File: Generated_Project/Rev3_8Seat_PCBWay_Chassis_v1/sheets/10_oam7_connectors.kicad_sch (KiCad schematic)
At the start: 0 parts

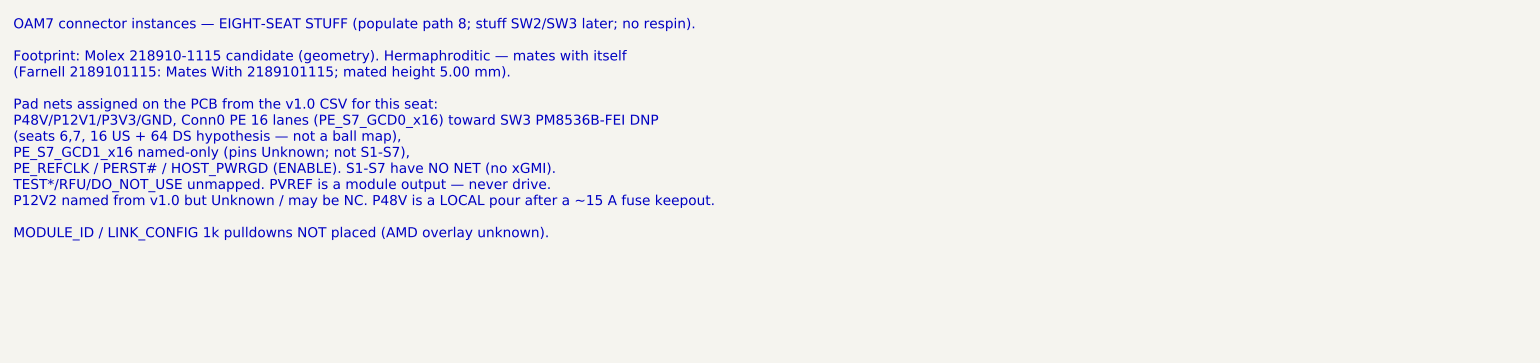
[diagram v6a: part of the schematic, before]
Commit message: Retarget Rev3 first article to seats 0-1 GCD0 x16 (2-module path).
Same 8-seat PCB. Without overlay, 2x MI250X means two modules can sit
and at most GCD0 on each can be named toward the host keepout (2 GCDs),
not 2x full-width (4 GCDs). Conn0 OCP PCIE_* is the only legal host PE.
No CEM/MCIO MPN. Do not energize P48V.

Co-authored-by: zivzancoeli-commits <zivzancoeli-commits@users.noreply.github.com>
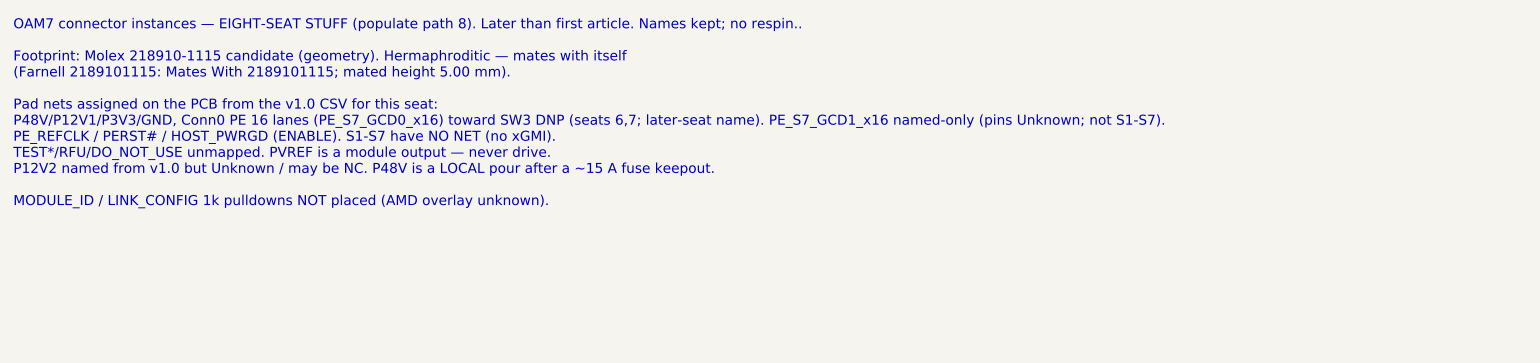
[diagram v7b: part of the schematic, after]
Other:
- note added: "OAM7 connector instances — EIGHT-SEAT STUFF (populate path 8). Later than first article. Names kept; no respin.. Footprint: Molex 218910-1115 candidate (geometry). Hermaphroditic — mates with itself (Farnell 2189101115: Mates With 2189101115; mated height 5.00 mm). Pad nets assigned on the PCB from the v1.0 CSV for this seat: P48V/P12V1/P3V3/GND, Conn0 PE 16 lanes (PE_S7_GCD0_x16) toward SW3 DNP 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"
- note removed: "OAM7 connector instances — EIGHT-SEAT STUFF (populate path 8; stuff SW2/SW3 later; no respin). Footprint: Molex 218910-1115 candidate (geometry). Hermaphroditic — mates with itself (Farnell 2189101115: Mates With 2189101115; mated height 5.00 mm). Pad nets assigned on the PCB from the v1.0 CSV for this seat: P48V/P12V1/P3V3/GND, Conn0 PE 16 lanes (PE_S7_GCD0_x16) toward SW3 PM8536B-FEI DNP (seats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"
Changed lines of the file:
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@@
         (comment 4 "r2.0 UNUSABLE. P3V3=Conn0 C1/C2. 12L 2.0mm stuffed-switch TARGET. 4x PM8536 DNP. Star-fed P48V.")
 	)
-	(text "OAM7 connector instances — EIGHT-SEAT STUFF (populate path 8; stuff SW2/SW3 later; no respin).\n\nFootprint: Molex 218910-1115 candidate (geometry). Hermaphroditic — mates with itself\n(Farnell 2189101115: Mates With 2189101115; mated height 5.00 mm).\n\nPad nets assigned on the PCB from the v1.0 CSV for this seat:\nP48V/P12V1/P3V3/GND, Conn0 PE 16 lanes (PE_S7_GCD0_x16) toward SW3 PM8536B-FEI DNP\n(seats 6,7, 16 US + 64 DS hypothesis — not a ball map),\nPE_S7_GCD1_x16 named-only (pins Unknown; not S1-S7),\nPE_REFCLK / PERST# / HOST_PWRGD (ENABLE). S1-S7 have NO NET (no xGMI).\nTEST*/RFU/DO_NOT_USE unmapped. PVREF is a module output — never drive.\nP12V2 named from v1.0 but Unknown / may be NC. P48V is a LOCAL pour after a ~15 A fuse keepout.\n\nMODULE_ID / LINK_CONFIG 1k pulldowns NOT placed (AMD overlay unknown).\n"
+	(text "OAM7 connector instances — EIGHT-SEAT STUFF (populate path 8). Later than first article. Names kept; no respin..\n\nFootprint: Molex 218910-1115 candidate (geometry). Hermaphroditic — mates with itself\n(Farnell 2189101115: Mates With 2189101115; mated height 5.00 mm).\n\nPad nets assigned on the PCB from the v1.0 CSV for this seat:\nP48V/P12V1/P3V3/GND, Conn0 PE 16 lanes (PE_S7_GCD0_x16) toward SW3 DNP (seats 6,7; later-seat name). PE_S7_GCD1_x16 named-only (pins Unknown; not S1-S7).\nPE_REFCLK / PERST# / HOST_PWRGD (ENABLE). S1-S7 have NO NET (no xGMI).\nTEST*/RFU/DO_NOT_USE unmapped. PVREF is a module output — never drive.\nP12V2 named from v1.0 but Unknown / may be NC. P48V is a LOCAL pour after a ~15 A fuse keepout.\n\nMODULE_ID / LINK_CONFIG 1k pulldowns NOT placed (AMD overlay unknown).\n"
 		(exclude_from_sim no)
 		(at 20.32 20.32 0)
